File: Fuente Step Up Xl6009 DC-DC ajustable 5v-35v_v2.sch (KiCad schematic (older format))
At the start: 7 parts, among them U1 XL6009E1

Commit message: Se realizan modificaciones sugeridas por el revisor
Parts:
- U1: symbol Fuente~Step~Up~Xl6009~DC-DC~ajustable~5v-35v_v2:XL6009E1 -> XL6009:XL6009E1
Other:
- moved on the sheet: C2
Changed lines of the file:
@@
 EESchema Schematic File Version 4
+LIBS:Fuente Step Up Xl6009 DC-DC ajustable 5v-35v_v2-cache
 EELAYER 30 0
 EELAYER END
@@
 L Device:CP C2
 U 1 1 5D877E2A
-P 7150 3000
-F 0 "C2" H 7268 3046 50  0000 L CNN
-F 1 "220 uF" H 7268 2955 50  0000 L CNN
-F 2 "" H 7188 2850 50  0001 C CNN
-F 3 "~" H 7150 3000 50  0001 C CNN
-	1    7150 3000
-	1    0    0    -1
-$EndComp
-$Comp
-L Fuente~Step~Up~Xl6009~DC-DC~ajustable~5v-35v_v2:XL6009E1 U1
+P 7100 3100
+F 0 "C2" H 7218 3146 50  0000 L CNN
+F 1 "220 uF" H 7218 3055 50  0000 L CNN
+F 2 "" H 7138 2950 50  0001 C CNN
+F 3 "~" H 7100 3100 50  0001 C CNN
+	1    7100 3100
+	1    0    0    -1
+$EndComp
+$Comp
+L XL6009:XL6009E1 U1
 U 1 1 5D87A8A4
 P 5450 3050
@@
 	6600 2350 6600 2900
 Wire Wire Line
-	7150 2350 7150 2850
-Wire Wire Line
-	6600 2350 7150 2350
+	6600 2350 7100 2350
 Connection ~ 6600 2350
 Wire Wire Line
@@
 	-1   0    0    1
 $EndComp
-Wire Wire Line
-	7150 3150 7150 3900
 $Comp
 L Device:CP C1
@@
 	6600 3700 6600 3900
 Wire Wire Line
-	6600 3900 7150 3900
+	6600 3900 7100 3900
 Wire Wire Line
 	4550 3400 4550 3050
@@
 L power:GND #PWR0102
 U 1 1 5D8B82F9
-P 5800 4050
-F 0 "#PWR0102" H 5800 3800 50  0001 C CNN
-F 1 "GND" H 5805 3877 50  0000 C CNN
-F 2 "" H 5800 4050 50  0001 C CNN
-F 3 "" H 5800 4050 50  0001 C CNN
-	1    5800 4050
+P 5800 4250
+F 0 "#PWR0102" H 5800 4000 50  0001 C CNN
+F 1 "GND" H 5805 4077 50  0000 C CNN
+F 2 "" H 5800 4250 50  0001 C CNN
+F 3 "" H 5800 4250 50  0001 C CNN
+	1    5800 4250
 	1    0    0    -1
 $EndComp
@@
 	1    0    0    -1
 $EndComp
-Wire Wire Line
-	5300 3900 5800 3900
 $Comp
 L power:PWR_FLAG #FLG0101
@@
 L power:PWR_FLAG #FLG0102
 U 1 1 5D919A44
-P 6100 4050
-F 0 "#FLG0102" H 6100 4125 50  0001 C CNN
-F 1 "PWR_FLAG" H 6100 4223 50  0000 C CNN
-F 2 "" H 6100 4050 50  0001 C CNN
-F 3 "~" H 6100 4050 50  0001 C CNN
-	1    6100 4050
+P 6150 4250
+F 0 "#FLG0102" H 6150 4325 50  0001 C CNN
+F 1 "PWR_FLAG" H 6150 4423 50  0000 C CNN
+F 2 "" H 6150 4250 50  0001 C CNN
+F 3 "~" H 6150 4250 50  0001 C CNN
+	1    6150 4250
 	-1   0    0    1
 $EndComp
 Wire Wire Line
-	5800 4050 5800 4000
+	7100 2950 7100 2350
+Wire Wire Line
+	5300 3900 5800 3900
+Wire Wire Line
+	5800 4250 5800 4000
 Connection ~ 5800 3900
 Wire Wire Line
 	5800 3900 6600 3900
 Wire Wire Line
-	6100 4050 6100 4000
-Wire Wire Line
-	6100 4000 5800 4000
+	6150 4000 5800 4000
+Wire Wire Line
+	6150 4000 6150 4250
 Connection ~ 5800 4000
 Wire Wire Line
 	5800 4000 5800 3900
+Wire Wire Line
+	7100 3250 7100 3900
 $EndSCHEMATC

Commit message: Se agregaron las carpetas Doc e Info
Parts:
- C1, C2: footprint (none) -> Capacitor_SMD:CP_Elec_10x10
- D1: footprint (none) -> SS34:SMB
- L1: footprint (none) -> Inductor_SMD:L_12x12mm_H8mm
- U1: footprint (none) -> SS34:SMA
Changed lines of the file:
@@
 F 0 "D1" H 6050 2450 50  0000 C CNN
 F 1 "SS34" H 6050 2250 50  0000 C CNN
-F 2 "" H 6050 2350 50  0001 C CNN
+F 2 "SS34:SMB" H 6050 2350 50  0001 C CNN
 F 3 "DO-214 ON Semiconductor" H 6050 2350 50  0001 L BNN
 F 4 "SS Series 500 mV 3 A 40 V Max Reverse Voltage Schottky Rectifier - DO-214AB" H 6050 2350 50  0001 L BNN "Field4"
@@
 F 0 "C2" H 7218 3146 50  0000 L CNN
 F 1 "220 uF" H 7218 3055 50  0000 L CNN
-F 2 "" H 7138 2950 50  0001 C CNN
+F 2 "Capacitor_SMD:CP_Elec_10x10" H 7138 2950 50  0001 C CNN
 F 3 "~" H 7100 3100 50  0001 C CNN
 	1    7100 3100
@@
 F 0 "U1" H 5994 3096 50  0000 L CNN
 F 1 "XL6009E1" H 5994 3005 50  0000 L CNN
-F 2 "" H 5150 3300 50  0001 C CNN
+F 2 "SS34:SMA" H 5150 3300 50  0001 C CNN
 F 3 "" H 5150 3300 50  0001 C CNN
 	1    5450 3050
@@
 F 0 "C1" H 4668 3596 50  0000 L CNN
 F 1 "220 uF" H 4668 3505 50  0000 L CNN
-F 2 "" H 4588 3400 50  0001 C CNN
+F 2 "Capacitor_SMD:CP_Elec_10x10" H 4588 3400 50  0001 C CNN
 F 3 "~" H 4550 3550 50  0001 C CNN
 	1    4550 3550
@@
 F 1 "1K" H 6670 3505 50  0000 L CNN
 F 2 "" V 6530 3550 50  0001 C CNN
-F 3 "~" H 6600 3550 50  0001 C CNN
+F 3 "Resistor_SMD:R_0805_2012Metric_Pad1.15x1.40mm_HandSolder" H 6600 3550 50  0001 C CNN
 	1    6600 3550
 	1    0    0    -1
@@
 F 0 "L1" V 5100 2350 50  0000 C CNN
 F 1 "330 mH" V 4900 2200 50  0000 L CNN
-F 2 "" H 5000 2350 50  0001 C CNN
+F 2 "Inductor_SMD:L_12x12mm_H8mm" H 5000 2350 50  0001 C CNN
 F 3 "~" H 5000 2350 50  0001 C CNN
 	1    5000 2350

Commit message: Se anadieron los footprints del regulador XL6009 y del potenciometro TH modelo 3296W
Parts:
- R1: footprint (none) -> Resistor_SMD:R_1806_4516Metric
- RV1: footprint (none) -> Potentiometer_THT:Potentiometer_Bourns_3296W_Vertical
- U1: footprint SS34:SMA -> LM2577:TO263-5
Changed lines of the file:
@@
 F 0 "U1" H 5994 3096 50  0000 L CNN
 F 1 "XL6009E1" H 5994 3005 50  0000 L CNN
-F 2 "SS34:SMA" H 5150 3300 50  0001 C CNN
+F 2 "LM2577:TO263-5" H 5150 3300 50  0001 C CNN
 F 3 "" H 5150 3300 50  0001 C CNN
 	1    5450 3050
@@
 F 0 "RV1" H 6530 3004 50  0000 R CNN
 F 1 "10K" H 6530 3095 50  0000 R CNN
-F 2 "" H 6600 3050 50  0001 C CNN
+F 2 "Potentiometer_THT:Potentiometer_Bourns_3296W_Vertical" H 6600 3050 50  0001 C CNN
 F 3 "~" H 6600 3050 50  0001 C CNN
 	1    6600 3050
@@
 F 0 "R1" H 6670 3596 50  0000 L CNN
 F 1 "1K" H 6670 3505 50  0000 L CNN
-F 2 "" V 6530 3550 50  0001 C CNN
+F 2 "Resistor_SMD:R_1806_4516Metric" V 6530 3550 50  0001 C CNN
 F 3 "Resistor_SMD:R_0805_2012Metric_Pad1.15x1.40mm_HandSolder" H 6600 3550 50  0001 C CNN
 	1    6600 3550

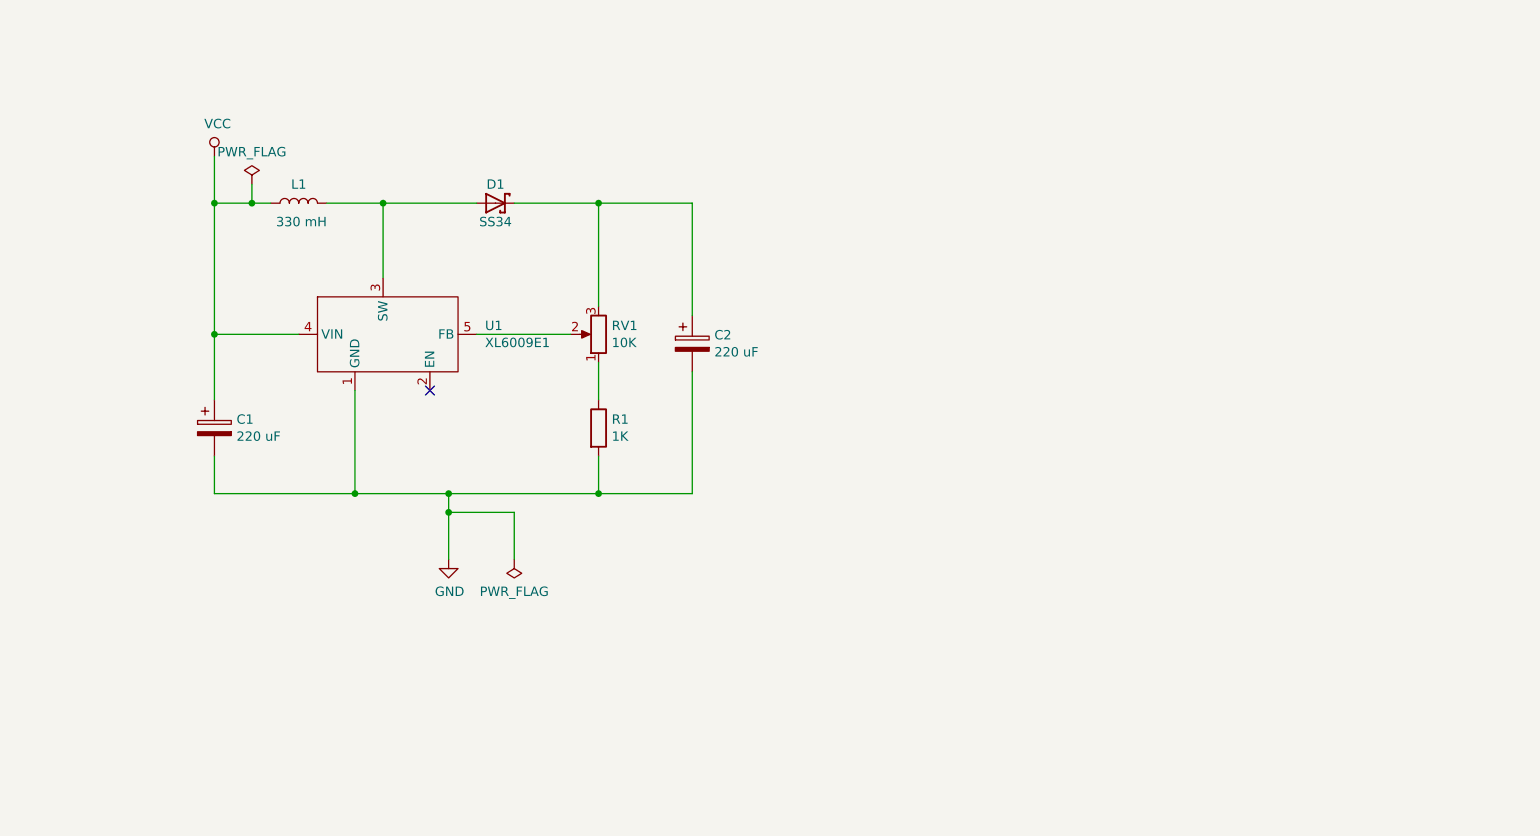
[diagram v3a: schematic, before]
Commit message: Se creo pcb y se hicieron modificaciones de acuerdo a recomendaciones del docente
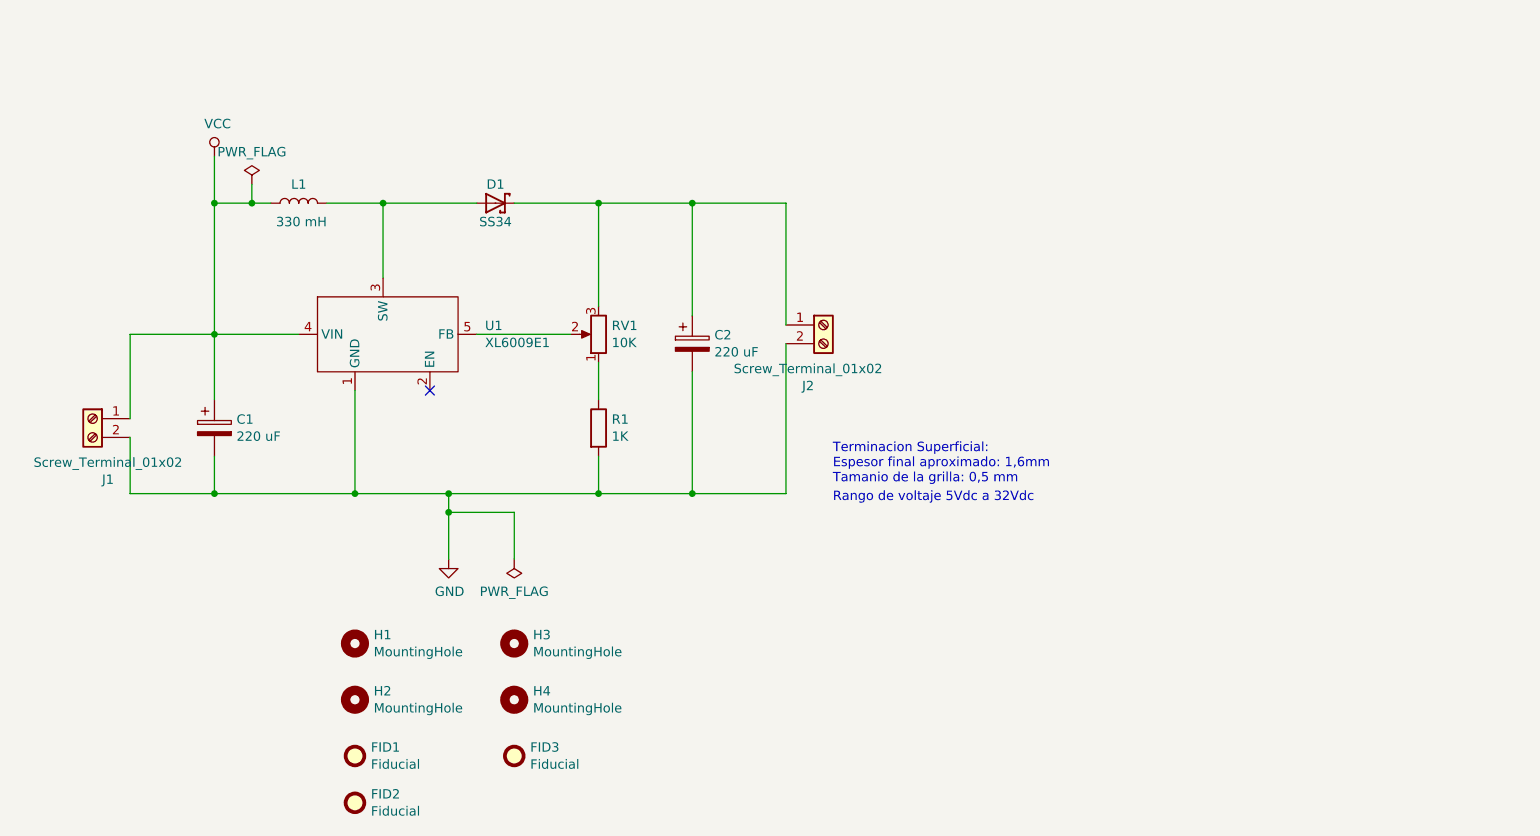
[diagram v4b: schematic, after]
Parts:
- added FID1, FID2, FID3: Fiducial, Fiducial:Fiducial_0.5mm_Mask1.5mm, symbol Mechanical:Fiducial
- added H1, H2, H3, H4: MountingHole, MountingHole:MountingHole_3.2mm_M3, symbol Mechanical:MountingHole
- added J1, J2: Screw_Terminal_01x02, TerminalBlock:TerminalBlock_Altech_AK300-2_P5.00mm, symbol Connector:Screw_Terminal_01x02
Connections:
- net GND: now also J1.2 (Pin_2), J2.2 (Pin_2)
- net VCC: now also J1.1 (Pin_1)
- net at C2.1, D1.C, RV1.3: now also J2.1 (Pin_1)
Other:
- note added: "Rango de voltaje 5Vdc a 32Vdc"
- note added: "Terminacion Superficial:\nEspesor final aproximado: 1,6mm\nTamanio de la grilla: 0,5 mm"
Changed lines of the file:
@@
 Sheet 1 1
 Title "Fuente Step Up Xl6009 DC-DC ajustable 5v-35v"
-Date "2019-09-22"
-Rev "0a"
+Date "2019-10-18"
+Rev "0b"
 Comp "Fabian Sarmiento"
-Comment1 ""
-Comment2 ""
+Comment1 "Realizado para la materia DCI de la Esp. en Sistemas Embebidos"
+Comment2 "Replica del modulo set-up adjustable boost converter. "
 Comment3 ""
 Comment4 ""
@@
 Wire Wire Line
 	7100 3250 7100 3900
+$Comp
+L Connector:Screw_Terminal_01x02 J1
+U 1 1 5DA12BD3
+P 3900 3500
+F 0 "J1" H 3818 3175 50  0000 C CNN
+F 1 "Screw_Terminal_01x02" H 3818 3266 50  0000 C CNN
+F 2 "TerminalBlock:TerminalBlock_Altech_AK300-2_P5.00mm" H 3900 3500 50  0001 C CNN
+F 3 "~" H 3900 3500 50  0001 C CNN
+	1    3900 3500
+	-1   0    0    -1
+$EndComp
+$Comp
+L Connector:Screw_Terminal_01x02 J2
+U 1 1 5DA178E6
+P 7800 3000
+F 0 "J2" H 7718 2675 50  0000 C CNN
+F 1 "Screw_Terminal_01x02" H 7718 2766 50  0000 C CNN
+F 2 "TerminalBlock:TerminalBlock_Altech_AK300-2_P5.00mm" H 7800 3000 50  0001 C CNN
+F 3 "~" H 7800 3000 50  0001 C CNN
+	1    7800 3000
+	1    0    0    -1
+$EndComp
+Wire Wire Line
+	4550 3050 4100 3050
+Wire Wire Line
+	4100 3050 4100 3500
+Wire Wire Line
+	4550 3900 4100 3900
+Wire Wire Line
+	4100 3900 4100 3600
+Connection ~ 4550 3900
+Wire Wire Line
+	7100 2350 7600 2350
+Wire Wire Line
+	7600 2350 7600 3000
+Connection ~ 7100 2350
+Wire Wire Line
+	7600 3100 7600 3900
+Wire Wire Line
+	7600 3900 7100 3900
+Connection ~ 7100 3900
+Text Notes 7850 3850 0    50   ~ 0
+Terminacion Superficial:\nEspesor final aproximado: 1,6mm\nTamanio de la grilla: 0,5 mm
+Text Notes 7850 3950 0    50   ~ 0
+Rango de voltaje 5Vdc a 32Vdc
+$Comp
+L Mechanical:MountingHole H1
+U 1 1 5DAB2C74
+P 5300 4700
+F 0 "H1" H 5400 4746 50  0000 L CNN
+F 1 "MountingHole" H 5400 4655 50  0000 L CNN
+F 2 "MountingHole:MountingHole_3.2mm_M3" H 5300 4700 50  0001 C CNN
+F 3 "~" H 5300 4700 50  0001 C CNN
+	1    5300 4700
+	1    0    0    -1
+$EndComp
+$Comp
+L Mechanical:MountingHole H3
+U 1 1 5DAB39CE
+P 6150 4700
+F 0 "H3" H 6250 4746 50  0000 L CNN
+F 1 "MountingHole" H 6250 4655 50  0000 L CNN
+F 2 "MountingHole:MountingHole_3.2mm_M3" H 6150 4700 50  0001 C CNN
+F 3 "~" H 6150 4700 50  0001 C CNN
+	1    6150 4700
+	1    0    0    -1
+$EndComp
+$Comp
+L Mechanical:MountingHole H2
+U 1 1 5DAB41E1
+P 5300 5000
+F 0 "H2" H 5400 5046 50  0000 L CNN
+F 1 "MountingHole" H 5400 4955 50  0000 L CNN
+F 2 "MountingHole:MountingHole_3.2mm_M3" H 5300 5000 50  0001 C CNN
+F 3 "~" H 5300 5000 50  0001 C CNN
+	1    5300 5000
+	1    0    0    -1
+$EndComp
+$Comp
+L Mechanical:MountingHole H4
+U 1 1 5DAB4871
+P 6150 5000
+F 0 "H4" H 6250 5046 50  0000 L CNN
+F 1 "MountingHole" H 6250 4955 50  0000 L CNN
+F 2 "MountingHole:MountingHole_3.2mm_M3" H 6150 5000 50  0001 C CNN
+F 3 "~" H 6150 5000 50  0001 C CNN
+	1    6150 5000
+	1    0    0    -1
+$EndComp
+$Comp
+L Mechanical:Fiducial FID1
+U 1 1 5DAC4F3C
+P 5300 5300
+F 0 "FID1" H 5385 5346 50  0000 L CNN
+F 1 "Fiducial" H 5385 5255 50  0000 L CNN
+F 2 "Fiducial:Fiducial_0.5mm_Mask1.5mm" H 5300 5300 50  0001 C CNN
+F 3 "~" H 5300 5300 50  0001 C CNN
+	1    5300 5300
+	1    0    0    -1
+$EndComp
+$Comp
+L Mechanical:Fiducial FID3
+U 1 1 5DAC61E3
+P 6150 5300
+F 0 "FID3" H 6235 5346 50  0000 L CNN
+F 1 "Fiducial" H 6235 5255 50  0000 L CNN
+F 2 "Fiducial:Fiducial_0.5mm_Mask1.5mm" H 6150 5300 50  0001 C CNN
+F 3 "~" H 6150 5300 50  0001 C CNN
+	1    6150 5300
+	1    0    0    -1
+$EndComp
+$Comp
+L Mechanical:Fiducial FID2
+U 1 1 5DAC6BFD
+P 5300 5550
+F 0 "FID2" H 5385 5596 50  0000 L CNN
+F 1 "Fiducial" H 5385 5505 50  0000 L CNN
+F 2 "Fiducial:Fiducial_0.5mm_Mask1.5mm" H 5300 5550 50  0001 C CNN
+F 3 "~" H 5300 5550 50  0001 C CNN
+	1    5300 5550
+	1    0    0    -1
+$EndComp
 $EndSCHEMATC

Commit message: Se modificaron las posiciones de los componentes de acuerdo a la recomencadion del companiero y se rutearon nuevamente algunas pistas
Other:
- note added: "Terminacion Superficial:\nEspesor final aproximado: 1,6mm\nTamanio de la grilla: 0,5 mm\nRango de voltaje 5Vdc a 32Vdc"
- note removed: "Terminacion Superficial:\nEspesor final aproximado: 1,6mm\nTamanio de la grilla: 0,5 mm"
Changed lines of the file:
@@
 Connection ~ 7100 3900
 Text Notes 7850 3850 0    50   ~ 0
-Terminacion Superficial:\nEspesor final aproximado: 1,6mm\nTamanio de la grilla: 0,5 mm
+Terminacion Superficial:\nEspesor final aproximado: 1,6mm\nTamanio de la grilla: 0,5 mm\nRango de voltaje 5Vdc a 32Vdc
 Text Notes 7850 3950 0    50   ~ 0
 Rango de voltaje 5Vdc a 32Vdc

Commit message: Se agregaron los codigos de los productos y se efectuaron las recomendaciones sugeridas por el companiero
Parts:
- C1, C2: Field4 (none) -> CAP ALUM 220UF 20% 50V SMD; Field5 (none) -> 493-2228-2-ND; Field7 (none) -> https://www.digikey.com/product-detail/en/nichicon/UWT1H221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
- D1: Field5 None -> SS34FSCT-ND; Field7 Unavailable -> https://www.digikey.com/product-detail/en/on-semiconductor/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
- R1: Field5 (none) -> 3296W-103-ND; Field7 (none) -> https://www.digikey.com/product-detail/en/bourns-inc/3296W-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
- U1: Field5 (none) -> 5249; Field7 (none) -> https://www.sunrom.com/p/xl6009e1-to263-5-ic-for-dc-dc-boost
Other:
- note added: "Replica desarrollada: https://www.nubbeo.com.ar/fuente-step-up-xl6009-dc-dc-ajustable-5v-35v-arduino-nubbeo-549561497xJM"
- note added: "Terminacion Superficial:\nEspesor final aproximado: 1,6mm\nTamanio de la grilla: 0,5 mm\n\nCaracterísticas:\nVoltaje de entrada: 3V-32V (voltaje óptimo 5V-32V)\nVoltaje de salida: 5-35V Ajustable\nIntensidad máxima de entrada: 4A ( se recomienda usar disipador térmico )\nIntensidad máxima de salida: 2A\nEficiencia aproximada: 94%\nFrecuencia de trabajo: 400KHz\nRango de temperatura trabajo: De -4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"
- note removed: "Rango de voltaje 5Vdc a 32Vdc"
- note removed: "Terminacion Superficial:\nEspesor final aproximado: 1,6mm\nTamanio de la grilla: 0,5 mm\nRango de voltaje 5Vdc a 32Vdc"
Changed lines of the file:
@@
 Rev "0b"
 Comp "Fabian Sarmiento"
-Comment1 "Realizado para la materia DCI de la Esp. en Sistemas Embebidos"
-Comment2 "Replica del modulo set-up adjustable boost converter. "
-Comment3 ""
+Comment1 "Revisores: Ivan Camilo Aranda, Jhonattan Camargo"
+Comment2 "Realizado para la materia DCI de la Esp. en Sistemas Embebidos"
+Comment3 "Replica del modulo set-up adjustable boost converter. "
 Comment4 ""
 $EndDescr
@@
 F 3 "DO-214 ON Semiconductor" H 6050 2350 50  0001 L BNN
 F 4 "SS Series 500 mV 3 A 40 V Max Reverse Voltage Schottky Rectifier - DO-214AB" H 6050 2350 50  0001 L BNN "Field4"
-F 5 "None" H 6050 2350 50  0001 L BNN "Field5"
+F 5 "SS34FSCT-ND" H 6050 2350 50  0001 L BNN "Field5"
 F 6 "SS34" H 6050 2350 50  0001 L BNN "Field6"
-F 7 "Unavailable" H 6050 2350 50  0001 L BNN "Field7"
+F 7 "https://www.digikey.com/product-detail/en/on-semiconductor/SS34/SS34FSCT-ND/2094459" H 6050 2350 50  0001 L BNN "Field7"
 F 8 "ON Semiconductor" H 6050 2350 50  0001 L BNN "Field8"
 	1    6050 2350
@@
 F 2 "Capacitor_SMD:CP_Elec_10x10" H 7138 2950 50  0001 C CNN
 F 3 "~" H 7100 3100 50  0001 C CNN
+F 4 "CAP ALUM 220UF 20% 50V SMD" H 7100 3100 50  0001 C CNN "Field4"
+F 5 "493-2228-2-ND" H 7100 3100 50  0001 C CNN "Field5"
+F 6 "https://www.digikey.com/product-detail/en/nichicon/UWT1H221MNL1GS/493-2228-2-ND/589969" H 7100 3100 50  0001 C CNN "Field7"
 	1    7100 3100
 	1    0    0    -1
@@
 F 2 "LM2577:TO263-5" H 5150 3300 50  0001 C CNN
 F 3 "" H 5150 3300 50  0001 C CNN
+F 4 "" H 5450 3050 50  0001 C CNN "Field6"
+F 5 "https://www.sunrom.com/p/xl6009e1-to263-5-ic-for-dc-dc-boost" H 5450 3050 50  0001 C CNN "Field7"
+F 6 "5249" H 5450 3050 50  0001 C CNN "Field5"
 	1    5450 3050
 	1    0    0    -1
@@
 F 2 "Capacitor_SMD:CP_Elec_10x10" H 4588 3400 50  0001 C CNN
 F 3 "~" H 4550 3550 50  0001 C CNN
+F 4 "CAP ALUM 220UF 20% 50V SMD" H 4550 3550 50  0001 C CNN "Field4"
+F 5 "493-2228-2-ND" H 4550 3550 50  0001 C CNN "Field5"
+F 6 "https://www.digikey.com/product-detail/en/nichicon/UWT1H221MNL1GS/493-2228-2-ND/589969" H 4550 3550 50  0001 C CNN "Field7"
 	1    4550 3550
 	1    0    0    -1
@@
 F 2 "Resistor_SMD:R_1806_4516Metric" V 6530 3550 50  0001 C CNN
 F 3 "Resistor_SMD:R_0805_2012Metric_Pad1.15x1.40mm_HandSolder" H 6600 3550 50  0001 C CNN
+F 4 "3296W-103-ND" H 6600 3550 50  0001 C CNN "Field5"
+F 5 "https://www.digikey.com/product-detail/en/bourns-inc/3296W-1-103/3296W-103-ND/84523" H 6600 3550 50  0001 C CNN "Field7"
 	1    6600 3550
 	1    0    0    -1
@@
 P 7800 3000
 F 0 "J2" H 7718 2675 50  0000 C CNN
-F 1 "Screw_Terminal_01x02" H 7718 2766 50  0000 C CNN
+F 1 "Screw_Terminal_01x02" V 7900 2950 50  0000 C CNN
 F 2 "TerminalBlock:TerminalBlock_Altech_AK300-2_P5.00mm" H 7800 3000 50  0001 C CNN
 F 3 "~" H 7800 3000 50  0001 C CNN
@@
 	7600 3900 7100 3900
 Connection ~ 7100 3900
-Text Notes 7850 3850 0    50   ~ 0
-Terminacion Superficial:\nEspesor final aproximado: 1,6mm\nTamanio de la grilla: 0,5 mm\nRango de voltaje 5Vdc a 32Vdc
-Text Notes 7850 3950 0    50   ~ 0
-Rango de voltaje 5Vdc a 32Vdc
 $Comp
 L Mechanical:MountingHole H1
@@
 	1    0    0    -1
 $EndComp
+Text Notes 7900 5200 0    50   ~ 0
+Terminacion Superficial:\nEspesor final aproximado: 1,6mm\nTamanio de la grilla: 0,5 mm\n\nCaracterísticas:\nVoltaje de entrada: 3V-32V (voltaje óptimo 5V-32V)\nVoltaje de salida:  5-35V Ajustable\nIntensidad máxima de entrada:  4A ( se recomienda usar disipador térmico )\nIntensidad máxima de salida: 2A\nEficiencia aproximada:   94%\nFrecuencia de trabajo:   400KHz\nRango de temperatura trabajo:  De -40 a +85 grados centígrados\nMedidas: 43mm x 21mm x 14mm
+Text Notes 3600 1450 0    59   ~ 0
+Replica desarrollada: https://www.nubbeo.com.ar/fuente-step-up-xl6009-dc-dc-ajustable-5v-35v-arduino-nubbeo-549561497xJM
 $EndSCHEMATC
